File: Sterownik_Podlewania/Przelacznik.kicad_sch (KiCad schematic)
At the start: 3 parts, among them SW2 SW_Nidec_CAS-120A1

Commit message: Poprawki estetyczne schematu
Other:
- moved on the sheet: C10
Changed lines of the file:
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@@
 	)
 	(junction
-		(at 156.21 109.22)
+		(at 143.51 96.52)
 		(diameter 0)
 		(color 0 0 0 0)
 	)
-	(wire
-		(pts
-			(xy 165.1 119.38) (xy 165.1 109.22)
-		)
-		(stroke
-			(width 0)
-			(type default)
-		)
-	)
-	(wire
-		(pts
-			(xy 133.35 99.06) (xy 132.08 99.06)
-		)
-		(stroke
-			(width 0)
-			(type default)
-		)
-	)
-	(wire
-		(pts
-			(xy 156.21 101.6) (xy 156.21 109.22)
+	(junction
+		(at 165.1 116.84)
+		(diameter 0)
+		(color 0 0 0 0)
+	)
+	(junction
+		(at 133.35 99.06)
+		(diameter 0)
+		(color 0 0 0 0)
+	)
+	(junction
+		(at 143.51 101.6)
+		(diameter 0)
+		(color 0 0 0 0)
+	)
+	(wire
+		(pts
+			(xy 133.35 99.06) (xy 123.19 99.06)
 		)
 		(stroke
@@
 	(wire
 		(pts
-			(xy 156.21 109.22) (xy 165.1 109.22)
+			(xy 143.51 101.6) (xy 165.1 101.6)
+		)
+		(stroke
+			(width 0)
+			(type default)
+		)
+	)
+	(wire
+		(pts
+			(xy 142.24 101.6) (xy 143.51 101.6)
+		)
+		(stroke
+			(width 0)
+			(type default)
+		)
+	)
+	(wire
+		(pts
+			(xy 133.35 113.03) (xy 133.35 116.84)
 		)
 		(stroke
@@
 	(wire
 		(pts
-			(xy 132.08 110.49) (xy 156.21 110.49)
-		)
-		(stroke
-			(width 0)
-			(type default)
-		)
-	)
-	(wire
-		(pts
-			(xy 143.51 101.6) (xy 156.21 101.6)
-		)
-		(stroke
-			(width 0)
-			(type default)
-		)
-	)
-	(wire
-		(pts
-			(xy 132.08 99.06) (xy 132.08 102.87)
-		)
-		(stroke
-			(width 0)
-			(type default)
-		)
-	)
-	(wire
-		(pts
-			(xy 165.1 81.28) (xy 165.1 82.55)
-		)
-		(stroke
-			(width 0)
-			(type default)
-		)
-	)
-	(wire
-		(pts
-			(xy 156.21 110.49) (xy 156.21 109.22)
+			(xy 142.24 96.52) (xy 143.51 96.52)
+		)
+		(stroke
+			(width 0)
+			(type default)
+		)
+	)
+	(wire
+		(pts
+			(xy 165.1 101.6) (xy 165.1 116.84)
+		)
+		(stroke
+			(width 0)
+			(type default)
+		)
+	)
+	(wire
+		(pts
+			(xy 133.35 99.06) (xy 133.35 105.41)
+		)
+		(stroke
+			(width 0)
+			(type default)
+		)
+	)
+	(wire
+		(pts
+			(xy 133.35 116.84) (xy 165.1 116.84)
+		)
+		(stroke
+			(width 0)
+			(type default)
+		)
+	)
+	(wire
+		(pts
+			(xy 165.1 73.66) (xy 165.1 82.55)
+		)
+		(stroke
+			(width 0)
+			(type default)
+		)
+	)
+	(wire
+		(pts
+			(xy 165.1 116.84) (xy 165.1 125.73)
 		)
 		(stroke
@@
 	(hierarchical_label "stan_przelacznika"
 		(shape output)
-		(at 132.08 99.06 180)
+		(at 123.19 99.06 180)
 		(effects
 			(font
@@
 			)
 			(justify right)
-		)
-	)
-	(rule_area
-		(polyline
-			(pts
-				(xy 179.705 72.7074) (xy 179.07 126.365) (xy 111.76 125.73) (xy 111.76 72.39)
-			)
-			(stroke
-				(width 0)
-				(type dash)
-			)
-			(fill
-				(type none)
-			)
 		)
 	)
@@
 					(unit 1)
 				)
+				(path "/a66bdf1f-0e2a-4cc5-beb1-605f2a3b9885/9a88e80e-3101-4c9e-b6e9-f6fd66520dd2/adff730d-5353-4d94-b665-43238fb73228"
+					(reference "R14")
+					(unit 1)
+				)
 				(path "/a66bdf1f-0e2a-4cc5-beb1-605f2a3b9885/aaafd38c-ffc0-4fc7-936b-5b26ec62426f/568b4e0a-513a-44c1-8d45-ad0443c3ee4b"
 					(reference "R24")
@@
 	(symbol
 		(lib_id "power:GND")
-		(at 165.1 119.38 0)
+		(at 165.1 125.73 0)
 		(unit 1)
 		(exclude_from_sim no)
@@
 		(fields_autoplaced yes)
 		(property "Reference" "#PWR063"
+			(at 165.1 132.08 0)
+			(effects
+				(font
+					(size 1.27 1.27)
+				)
+				(hide yes)
+			)
+		)
+		(property "Value" "GND"
+			(at 165.1 130.81 0)
+			(effects
+				(font
+					(size 1.27 1.27)
+				)
+			)
+		)
+		(property "Footprint" ""
 			(at 165.1 125.73 0)
 			(effects
@@
 			)
 		)
-		(property "Value" "GND"
-			(at 165.1 124.46 0)
-			(effects
-				(font
-					(size 1.27 1.27)
-				)
-			)
-		)
-		(property "Footprint" ""
-			(at 165.1 119.38 0)
-			(effects
-				(font
-					(size 1.27 1.27)
-				)
-				(hide yes)
-			)
-		)
 		(property "Datasheet" ""
-			(at 165.1 119.38 0)
+			(at 165.1 125.73 0)
 			(effects
 				(font
@@
 		)
 		(property "Description" "Power symbol creates a global label with name \"GND\" , ground"
-			(at 165.1 119.38 0)
+			(at 165.1 125.73 0)
 			(effects
 				(font
@@
 					(unit 1)
 				)
+				(path "/a66bdf1f-0e2a-4cc5-beb1-605f2a3b9885/9a88e80e-3101-4c9e-b6e9-f6fd66520dd2/adff730d-5353-4d94-b665-43238fb73228"
+					(reference "#PWR044")
+					(unit 1)
+				)
 				(path "/a66bdf1f-0e2a-4cc5-beb1-605f2a3b9885/aaafd38c-ffc0-4fc7-936b-5b26ec62426f/568b4e0a-513a-44c1-8d45-ad0443c3ee4b"
 					(reference "#PWR067")
@@
 	(symbol
 		(lib_id "Device:C")
-		(at 132.08 106.68 0)
+		(at 133.35 109.22 0)
 		(unit 1)
 		(exclude_from_sim no)
@@
 		(fields_autoplaced yes)
 		(property "Reference" "C10"
-			(at 135.89 105.4099 0)
+			(at 137.16 107.9499 0)
 			(effects
 				(font
@@
 		)
 		(property "Value" "0.1u"
-			(at 135.89 107.9499 0)
+			(at 137.16 110.4899 0)
 			(effects
 				(font
@@
 		)
 		(property "Footprint" "Capacitor_SMD:C_1206_3216Metric"
-			(at 133.0452 110.49 0)
+			(at 134.3152 113.03 0)
 			(effects
 				(font
@@
 		)
 		(property "Datasheet" "~"
-			(at 132.08 106.68 0)
+			(at 133.35 109.22 0)
 			(effects
 				(font
@@
 		)
 		(property "Description" "Unpolarized capacitor"
-			(at 132.08 106.68 0)
+			(at 133.35 109.22 0)
 			(effects
 				(font
@@
 					(unit 1)
 				)
+				(path "/a66bdf1f-0e2a-4cc5-beb1-605f2a3b9885/9a88e80e-3101-4c9e-b6e9-f6fd66520dd2/adff730d-5353-4d94-b665-43238fb73228"
+					(reference "C1")
+					(unit 1)
+				)
 				(path "/a66bdf1f-0e2a-4cc5-beb1-605f2a3b9885/aaafd38c-ffc0-4fc7-936b-5b26ec62426f/568b4e0a-513a-44c1-8d45-ad0443c3ee4b"
 					(reference "C12")
@@
 	(symbol
 		(lib_id "power:+5V")
-		(at 165.1 81.28 0)
+		(at 165.1 73.66 0)
 		(unit 1)
 		(exclude_from_sim no)
@@
 		(fields_autoplaced yes)
 		(property "Reference" "#PWR062"
-			(at 165.1 85.09 0)
+			(at 165.1 77.47 0)
 			(effects
 				(font
@@
 		)
 		(property "Value" "+3.3V"
-			(at 165.1 76.2 0)
+			(at 165.1 68.58 0)
 			(effects
 				(font
@@
 		)
 		(property "Footprint" ""
-			(at 165.1 81.28 0)
+			(at 165.1 73.66 0)
 			(effects
 				(font
@@
 		)
 		(property "Datasheet" ""
-			(at 165.1 81.28 0)
+			(at 165.1 73.66 0)
 			(effects
 				(font
@@
 		)
 		(property "Description" "Power symbol creates a global label with name \"+5V\""
-			(at 165.1 81.28 0)
+			(at 165.1 73.66 0)
 			(effects
 				(font
@@
 				(path "/a66bdf1f-0e2a-4cc5-beb1-605f2a3b9885/995f053e-6bfd-4935-9460-d34c9e8248bd/568b4e0a-513a-44c1-8d45-ad0443c3ee4b"
 					(reference "#PWR070")
+					(unit 1)
+				)
+				(path "/a66bdf1f-0e2a-4cc5-beb1-605f2a3b9885/9a88e80e-3101-4c9e-b6e9-f6fd66520dd2/adff730d-5353-4d94-b665-43238fb73228"
+					(reference "#PWR043")
 					(unit 1)
 				)
@@
 					(unit 1)
 				)
+				(path "/a66bdf1f-0e2a-4cc5-beb1-605f2a3b9885/9a88e80e-3101-4c9e-b6e9-f6fd66520dd2/adff730d-5353-4d94-b665-43238fb73228"
+					(reference "SW9")
+					(unit 1)
+				)

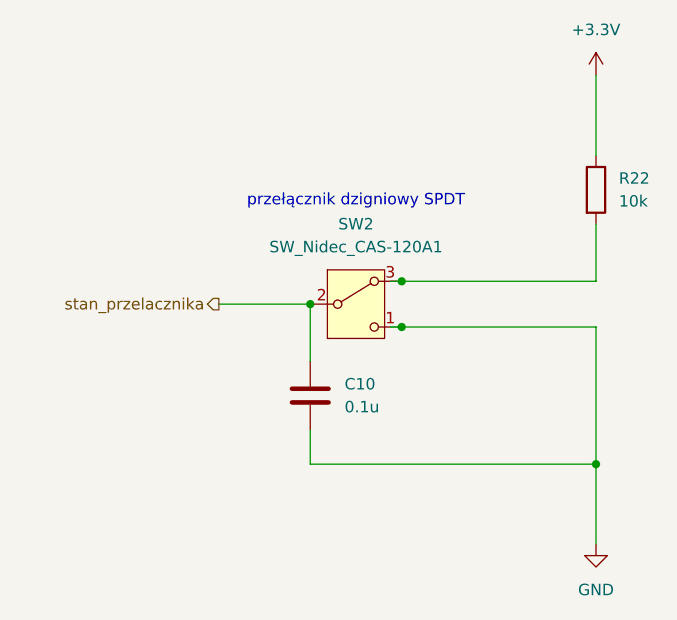
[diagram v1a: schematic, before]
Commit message: Dodanie gniazd ethernet, poprawienie większośc ERC
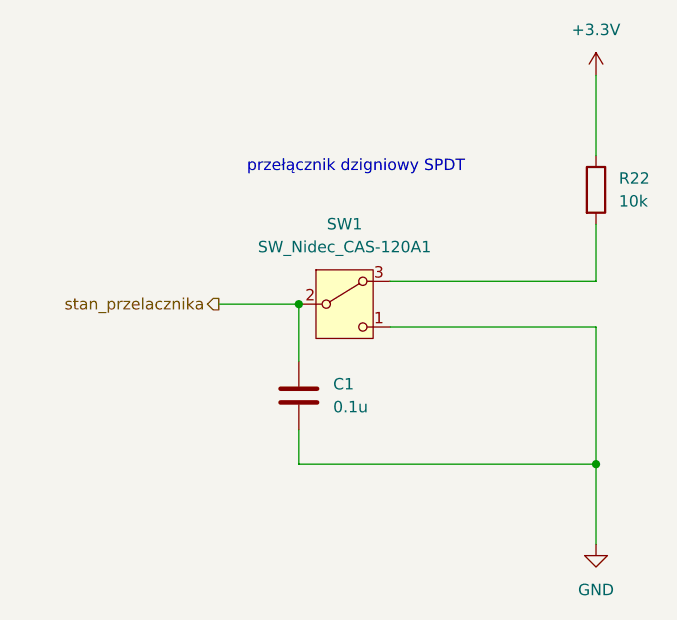
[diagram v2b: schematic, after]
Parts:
- renumbered C10 to C1, SW2 to SW1
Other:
- moved on the sheet: C1, SW1

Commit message: Dodanie modeli 3d, nowy footprint do przełącznika, przerzucenie na drugą stronę płytki elementów, wstępne rozdzielenie elemntów pasywnych
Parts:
- SW1: footprint Button_Switch_SMD:Nidec_Copal_CAS-120A -> Toggle_Switch:Toggle Switch Bootland 4.7mm
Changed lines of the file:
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@@
 			)
 		)
-		(property "Footprint" "Button_Switch_SMD:Nidec_Copal_CAS-120A"
+		(property "Footprint" "Toggle_Switch:Toggle Switch Bootland 4.7mm"
 			(at 137.16 109.22 0)
 			(effects
